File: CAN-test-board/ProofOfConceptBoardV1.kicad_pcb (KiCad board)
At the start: 2 copper layers, 42 parts, among them U1 MCP2515-EST, U2 MCP2515-EST

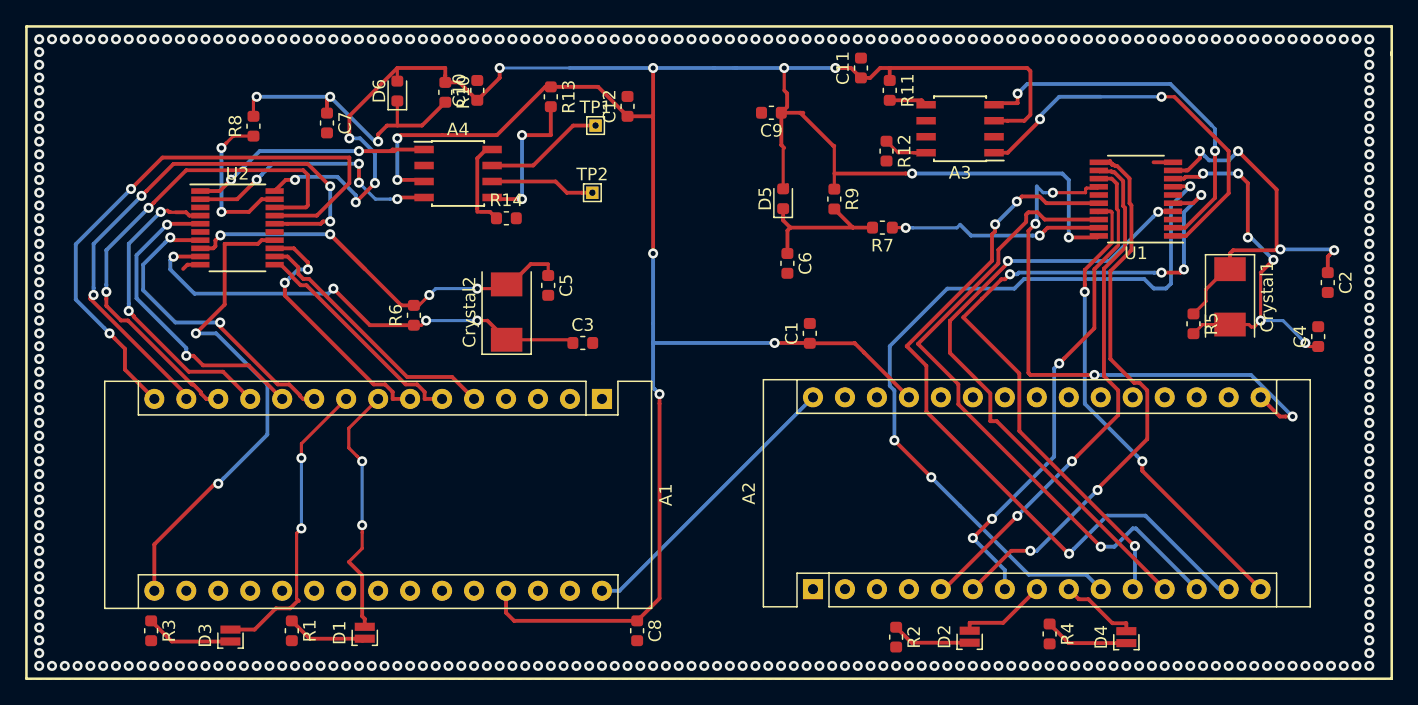
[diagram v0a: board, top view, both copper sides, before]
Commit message: CAN Test Board B1.0.1 Shrink to <10cm^2 for printing
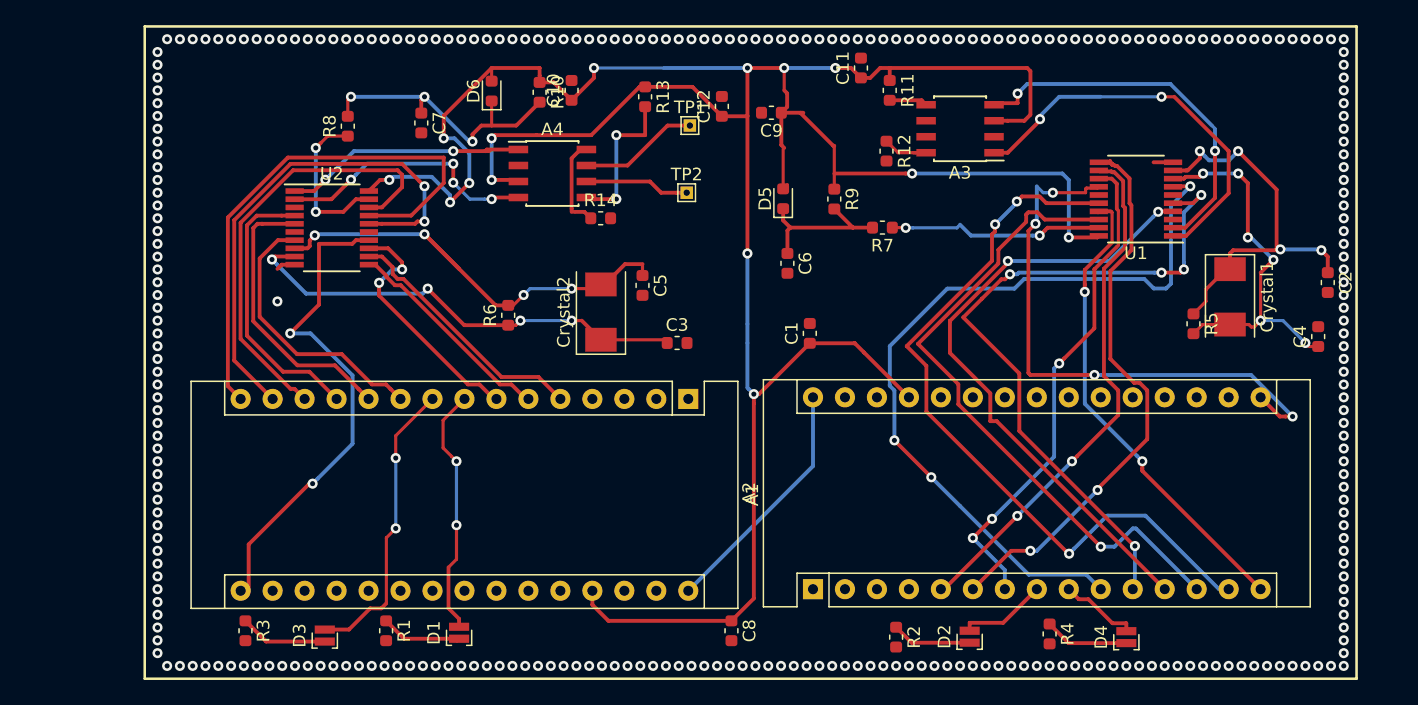
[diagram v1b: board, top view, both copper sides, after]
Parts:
- moved Crystal2 7.49 mm to (114.7, 79.3)
- moved D3 7.49 mm to (92.8, 105.0)
- moved R10 7.49 mm to (109.9, 61.9)
- moved R14 7.49 mm to (114.7, 71.9)
- moved R6 7.49 mm to (107.4, 79.6)
- moved TP1 7.49 mm to (121.8, 64.5)
- moved A4 7.49 mm to (110.9, 68.3)
- moved C10 7.49 mm to (112.4, 61.7)
- moved C12 7.49 mm to (124.3, 63.0)
- moved C3 7.49 mm to (120.8, 81.8)
- moved C5 7.49 mm to (118.0, 77.2)
- moved C7 7.49 mm to (100.5, 64.3)
- moved C8 7.49 mm to (125.1, 104.6)
- moved D1 7.49 mm to (103.5, 104.8)
- moved D6 7.49 mm to (106.0, 61.8)
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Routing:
- net +5V: track 239.8 -> 226.0 mm, vias 15 -> 14
- net MISO_2: track 48.5 -> 43.0 mm, vias 2 -> 0
- net SS_2: track 40.4 -> 35.3 mm, vias 2 -> 0
- net MOSI_2: track 45.2 -> 40.5 mm, vias 4 -> 2
- net TBUF0_2: track 26.1 -> 21.9 mm, vias 2 -> 0
- net VCC: track 23.1 -> 19.5 mm
- net TBUF2_2: track 25.1 -> 22.1 mm, vias 2 -> 0
- net TBUF1_2: track 24.8 -> 22.5 mm, vias 2 -> 0
- net OSC1_2: track 38.4 -> 36.7 mm
- net INT1_2: track 18.1 -> 16.9 mm
- net OSC1: track 34.7 -> 33.7 mm
- net INTMCP_2: track 20.6 -> 19.7 mm
- net Net-(A1-Pad9): track 24.2 -> 23.5 mm
- net INT0_2: track 20.8 -> 20.2 mm
- net Net-(A1-Pad8): track 20.5 -> 19.9 mm
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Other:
- board text added: "Missouri S&T Underwater Robotics Team CAN Protocol / Driver Testing Board Jack Juang | S1.0.0 B1.0.1"
- board text removed: "Missouri S&T Underwater Robotics Team CAN Protocol / Driver Testing Board Jack Juang | S1.0.0 B1.0.0"
